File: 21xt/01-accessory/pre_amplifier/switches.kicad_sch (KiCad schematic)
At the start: 0 parts

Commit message: completed schemtic
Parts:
- added C23, C26, C28, C30, C32, C34, C36, C38, C40, C42, C44, C46, C48, C50, C52, C54: 1uF, symbol Device:C
- added C24, C25, C27, C29, C31, C33, C35, C37, C39, C41, C43, C45, C47, C49, C51, C53: 10nF, symbol Device:C
- added IC13, IC14, IC15, IC16, IC17, IC18, IC19, IC20: MAX14774ATP+, QFN50P400X400X80-21N, symbol 21xt_preamp-symbols:MAX14774ATP+
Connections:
- new net: C24.2, IC13.1 (VP)
- new net: C37.2, IC16.1 (VP)
- new net: C35.1, IC16.3 (VN)
- new net: C45.2, IC18.1 (VP)
- new net: C43.1, IC18.3 (VN)
- new net: C29.2, IC14.1 (VP)
- new net: C39.1, IC17.3 (VN)
- new net: C25.1, IC13.3 (VN)
- new net: C41.2, IC17.1 (VP)
- new net: C33.2, IC15.1 (VP)
- new net: C49.2, IC19.1 (VP)
- new net: C47.1, IC19.3 (VN)
- new net: C51.1, IC20.3 (VN)
- new net: C31.1, IC15.3 (VN)
- new net: C27.1, IC14.3 (VN)
- new net: C53.2, IC20.1 (VP)
- new net 5V: C23.1, C26.1, C28.1, C30.1, C32.1, C34.1, C36.1, C38.1, C40.1, C42.1, C44.1, C46.1, C48.1, C50.1, C52.1, C54.1, IC13.13 (VL), IC13.4 (VCC), IC14.13 (VL), IC14.4 (VCC), IC15.13 (VL), IC15.4 (VCC), IC16.13 (VL), IC16.4 (VCC), IC17.13 (VL), IC17.4 (VCC), IC18.13 (VL), IC18.4 (VCC), IC19.13 (VL), IC19.4 (VCC), IC20.13 (VL), IC20.4 (VCC)
- new net GND: C23.2, C24.1, C25.2, C26.2, C27.2, C28.2, C29.1, C30.2, C31.2, C32.2, C33.1, C34.2, C35.2, C36.2, C37.1, C38.2, C39.2, C40.2, C41.1, C42.2, C43.2, C44.2, C45.1, C46.2, C47.2, C48.2, C49.1, C50.2, C51.2, C52.2, C53.1, C54.2, IC13.2 (GND_1), IC13.21 (GND_2), IC13.5 (I.C.), IC14.2 (GND_1), IC14.21 (GND_2), IC14.5 (I.C.), IC15.2 (GND_1), IC15.21 (GND_2), IC15.5 (I.C.), IC16.2 (GND_1), IC16.21 (GND_2), IC16.5 (I.C.), IC17.2 (GND_1), IC17.21 (GND_2), IC17.5 (I.C.), IC18.2 (GND_1), IC18.21 (GND_2), IC18.5 (I.C.), IC19.2 (GND_1), IC19.21 (GND_2), IC19.5 (I.C.), IC20.2 (GND_1), IC20.21 (GND_2), IC20.5 (I.C.)
- new net P12: IC20.11 (EN1)
- new net P124_2: IC16.11 (EN1)
- new net P12_2: IC13.11 (EN1)
- new net P13: IC20.12 (EN2)
- new net P13_2: IC13.12 (EN2)
- new net P14: IC20.14 (EN3)
- new net P14_2: IC13.14 (EN3)
- new net P15: IC20.15 (EN4)
- new net P15_2: IC13.15 (EN4)
- new net P16: IC19.11 (EN1)
- new net P16_2: IC14.11 (EN1)
- new net P17: IC19.12 (EN2)
- new net P17_2: IC14.12 (EN2)
- new net P18: IC19.14 (EN3)
- new net P18_2: IC14.14 (EN3)
- new net P19: IC19.15 (EN4)
- new net P19_2: IC14.15 (EN4)
- new net P20: IC18.11 (EN1)
- new net P20_2: IC15.11 (EN1)
- new net P21: IC18.12 (EN2)
- new net P21_2: IC15.12 (EN2)
- new net P22_2: IC15.14 (EN3)
- new net P23_2: IC15.15 (EN4)
- new net P25_2: IC16.12 (EN2)
- new net P26_2: IC16.14 (EN3)
- new net P27_2: IC16.15 (EN4)
- new net P28_2: IC17.11 (EN1)
- new net P29_2: IC17.12 (EN2)
- new net P30_2: IC17.14 (EN3)
- new net P31_2: IC17.15 (EN4)
- new net Rg10_y: IC18.7 (A2)
- new net Rg10_z: IC18.19 (B2)
- new net Rg1_y: IC20.6 (A1)
- new net Rg1_z: IC20.20 (B1)
- new net Rg2_y: IC20.7 (A2)
- new net Rg2_z: IC20.19 (B2)
- new net Rg3_y: IC20.8 (A3)
- new net Rg3_z: IC20.18 (B3)
- new net Rg4_y: IC20.9 (A4)
- new net Rg4_z: IC20.17 (B4)
- new net Rg5_y: IC19.6 (A1)
- new net Rg5_z: IC19.20 (B1)
- new net Rg6_y: IC19.7 (A2)
- new net Rg6_z: IC19.19 (B2)
- new net Rg7_y: IC19.8 (A3)
- new net Rg7_z: IC19.18 (B3)
- new net Rg8_y: IC19.9 (A4)
- new net Rg8_z: IC19.17 (B4)
- new net Rg9_y: IC18.6 (A1)
- new net Rg9_z: IC18.20 (B1)
- new net Switch_x1: IC13.6 (A1)
- new net Switch_x10: IC15.7 (A2)
- new net Switch_x11: IC15.8 (A3)
- new net Switch_x12: IC15.9 (A4)
- new net Switch_x13: IC16.6 (A1)
- new net Switch_x14: IC16.7 (A2)
- new net Switch_x15: IC16.8 (A3)
- new net Switch_x16: IC16.9 (A4)
- new net Switch_x17: IC17.6 (A1)
- new net Switch_x18: IC17.7 (A2)
- new net Switch_x19: IC17.8 (A3)
- new net Switch_x2: IC13.7 (A2)
- new net Switch_x20: IC17.9 (A4)
- new net Switch_x3: IC13.8 (A3)
- new net Switch_x4: IC13.9 (A4)
- new net Switch_x5: IC14.6 (A1)
- new net Switch_x6: IC14.7 (A2)
- new net Switch_x7: IC14.8 (A3)
- new net Switch_x8: IC14.9 (A4)
- new net Switch_x9: IC15.6 (A1)
- new net Switch_y1: IC13.20 (B1)
- new net Switch_y10: IC15.19 (B2)
- new net Switch_y11: IC15.18 (B3)
- new net Switch_y12: IC15.17 (B4)
- new net Switch_y13: IC16.20 (B1)
- new net Switch_y14: IC16.19 (B2)
- new net Switch_y15: IC16.18 (B3)
- new net Switch_y16: IC16.17 (B4)
- new net Switch_y17: IC17.20 (B1)
- new net Switch_y18: IC17.19 (B2)
- new net Switch_y19: IC17.18 (B3)
- new net Switch_y2: IC13.19 (B2)
- new net Switch_y20: IC17.17 (B4)
- new net Switch_y3: IC13.18 (B3)
- new net Switch_y4: IC13.17 (B4)
- new net Switch_y5: IC14.20 (B1)
- new net Switch_y6: IC14.19 (B2)
- new net Switch_y7: IC14.18 (B3)
- new net Switch_y8: IC14.17 (B4)
- new net Switch_y9: IC15.20 (B1)
- no-connect marks 0 -> 22

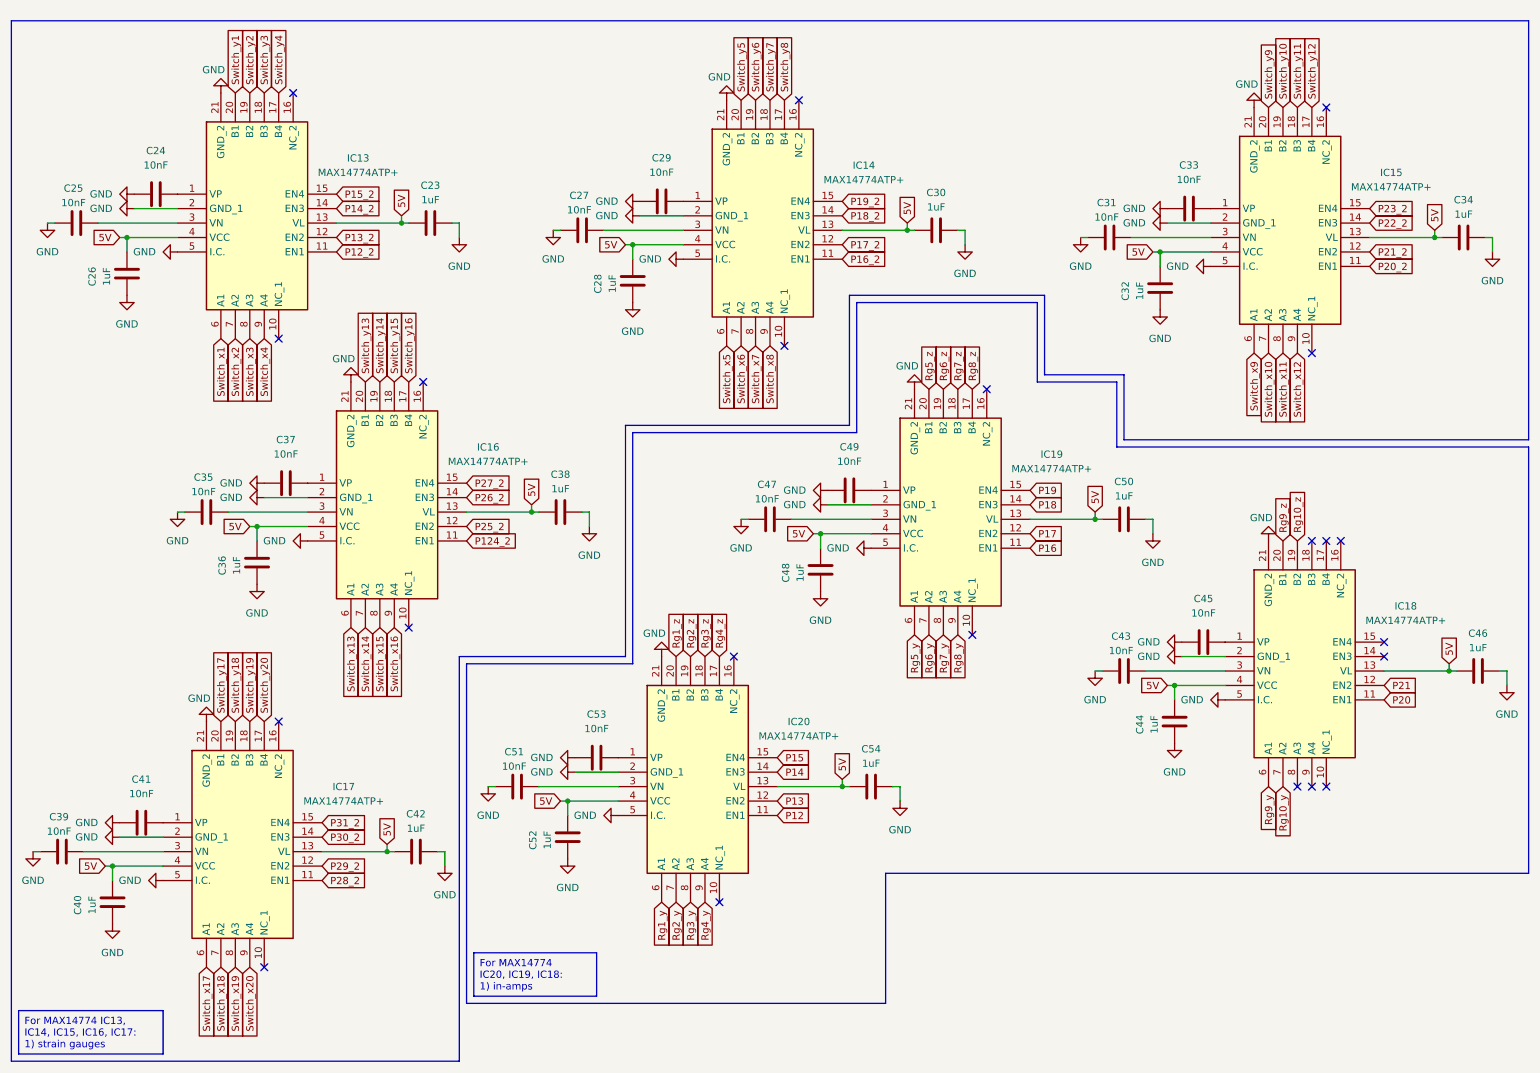
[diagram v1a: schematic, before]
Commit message: Reviewed schematic
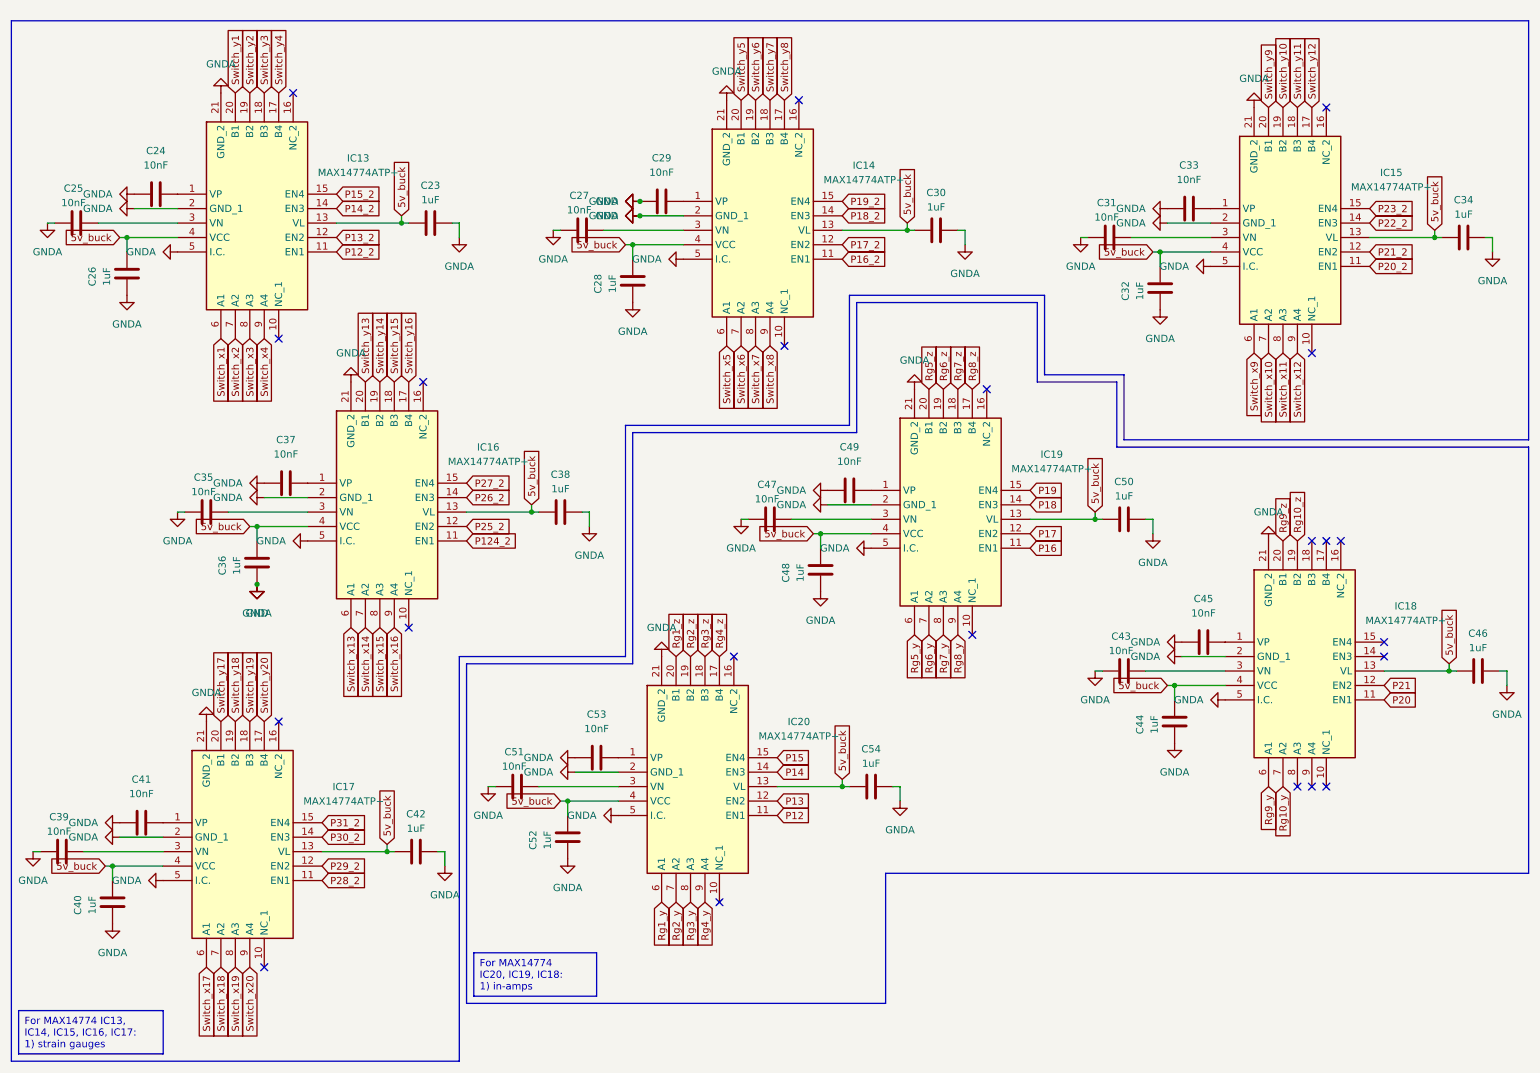
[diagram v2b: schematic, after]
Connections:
- net 5V renamed 5v_buck

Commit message: added footprints
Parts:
- IC13, IC14, IC15, IC16, IC17, IC18, IC19, IC20: footprint QFN50P400X400X80-21N -> pre_amp_footprint_lib:MAX14774ATP+_footprint
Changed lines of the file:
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@@
 			)
 		)
-		(property "Footprint" "QFN50P400X400X80-21N"
+		(property "Footprint" "pre_amp_footprint_lib:MAX14774ATP+_footprint"
 			(at 252.73 207.95 0)
 			(effects
@@
 			)
 		)
-		(property "Footprint" "QFN50P400X400X80-21N"
+		(property "Footprint" "pre_amp_footprint_lib:MAX14774ATP+_footprint"
 			(at 91.44 180.01 0)
 			(effects
@@
 			)
 		)
-		(property "Footprint" "QFN50P400X400X80-21N"
+		(property "Footprint" "pre_amp_footprint_lib:MAX14774ATP+_footprint"
 			(at 68.58 129.21 0)
 			(effects
@@
 			)
 		)
-		(property "Footprint" "QFN50P400X400X80-21N"
+		(property "Footprint" "pre_amp_footprint_lib:MAX14774ATP+_footprint"
 			(at 190.5 181.28 0)
 			(effects
@@
 			)
 		)
-		(property "Footprint" "QFN50P400X400X80-21N"
+		(property "Footprint" "pre_amp_footprint_lib:MAX14774ATP+_footprint"
 			(at 66.04 239.7 0)
 			(effects
@@
 			)
 		)
-		(property "Footprint" "QFN50P400X400X80-21N"
+		(property "Footprint" "pre_amp_footprint_lib:MAX14774ATP+_footprint"
 			(at 250.19 131.75 0)
 			(effects
@@
 			)
 		)
-		(property "Footprint" "QFN50P400X400X80-21N"
+		(property "Footprint" "pre_amp_footprint_lib:MAX14774ATP+_footprint"
 			(at 157.48 130.48 0)
 			(effects
@@
 			)
 		)
-		(property "Footprint" "QFN50P400X400X80-21N"
+		(property "Footprint" "pre_amp_footprint_lib:MAX14774ATP+_footprint"
 			(at 146.05 228.27 0)
 			(effects

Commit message: added footprints
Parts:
- IC13, IC14, IC15, IC16, IC17, IC18, IC19, IC20: footprint pre_amp_footprint_lib:MAX14774ATP+_footprint -> 21xt_footprints:MAX14774ATP_
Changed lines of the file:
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@@
 			)
 		)
-		(property "Footprint" "pre_amp_footprint_lib:MAX14774ATP+_footprint"
+		(property "Footprint" "21xt_footprints:MAX14774ATP_"
 			(at 252.73 207.95 0)
 			(effects
@@
 			)
 		)
-		(property "Footprint" "pre_amp_footprint_lib:MAX14774ATP+_footprint"
+		(property "Footprint" "21xt_footprints:MAX14774ATP_"
 			(at 91.44 180.01 0)
 			(effects
@@
 			)
 		)
-		(property "Footprint" "pre_amp_footprint_lib:MAX14774ATP+_footprint"
+		(property "Footprint" "21xt_footprints:MAX14774ATP_"
 			(at 68.58 129.21 0)
 			(effects
@@
 			)
 		)
-		(property "Footprint" "pre_amp_footprint_lib:MAX14774ATP+_footprint"
+		(property "Footprint" "21xt_footprints:MAX14774ATP_"
 			(at 190.5 181.28 0)
 			(effects
@@
 			)
 		)
-		(property "Footprint" "pre_amp_footprint_lib:MAX14774ATP+_footprint"
+		(property "Footprint" "21xt_footprints:MAX14774ATP_"
 			(at 66.04 239.7 0)
 			(effects
@@
 			)
 		)
-		(property "Footprint" "pre_amp_footprint_lib:MAX14774ATP+_footprint"
+		(property "Footprint" "21xt_footprints:MAX14774ATP_"
 			(at 250.19 131.75 0)
 			(effects
@@
 			)
 		)
-		(property "Footprint" "pre_amp_footprint_lib:MAX14774ATP+_footprint"
+		(property "Footprint" "21xt_footprints:MAX14774ATP_"
 			(at 157.48 130.48 0)
 			(effects
@@
 			)
 		)
-		(property "Footprint" "pre_amp_footprint_lib:MAX14774ATP+_footprint"
+		(property "Footprint" "21xt_footprints:MAX14774ATP_"
 			(at 146.05 228.27 0)
 			(effects

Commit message: assigned footprints
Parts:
- C23, C24, C25, C26, C27, C28, C29, C30, C31, C32, C33, C34, C35, C36, C37, C38, C39, C40, C41, C42, C43, C44, C45, C46, C47, C48, C49, C50, C51, C52, C53, C54: footprint (none) -> Capacitor_SMD:C_0402_1005Metric
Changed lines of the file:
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@@
 			)
 		)
-		(property "Footprint" ""
+		(property "Footprint" "Capacitor_SMD:C_0402_1005Metric"
 			(at 36.5252 62.23 0)
 			(effects
@@
 			)
 		)
-		(property "Footprint" ""
+		(property "Footprint" "Capacitor_SMD:C_0402_1005Metric"
 			(at 44.45 43.4848 0)
 			(effects
@@
 			)
 		)
-		(property "Footprint" ""
+		(property "Footprint" "Capacitor_SMD:C_0402_1005Metric"
 			(at 67.31 94.2848 0)
 			(effects
@@
 			)
 		)
-		(property "Footprint" ""
+		(property "Footprint" "Capacitor_SMD:C_0402_1005Metric"
 			(at 181.61 49.8348 0)
 			(effects
@@
 			)
 		)
-		(property "Footprint" ""
+		(property "Footprint" "Capacitor_SMD:C_0402_1005Metric"
 			(at 45.72 101.2952 0)
 			(effects
@@
 			)
 		)
-		(property "Footprint" ""
+		(property "Footprint" "Capacitor_SMD:C_0402_1005Metric"
 			(at 133.35 44.7548 0)
 			(effects
@@
 			)
 		)
-		(property "Footprint" ""
+		(property "Footprint" "Capacitor_SMD:C_0402_1005Metric"
 			(at 113.9952 161.29 0)
 			(effects
@@
 			)
 		)
-		(property "Footprint" ""
+		(property "Footprint" "Capacitor_SMD:C_0402_1005Metric"
 			(at 228.6 122.2248 0)
 			(effects
@@
 			)
 		)
-		(property "Footprint" ""
+		(property "Footprint" "Capacitor_SMD:C_0402_1005Metric"
 			(at 276.86 127.3048 0)
 			(effects
@@
 			)
 		)
-		(property "Footprint" ""
+		(property "Footprint" "Capacitor_SMD:C_0402_1005Metric"
 			(at 115.57 99.3648 0)
 			(effects
@@
 			)
 		)
-		(property "Footprint" ""
+		(property "Footprint" "Capacitor_SMD:C_0402_1005Metric"
 			(at 20.32 160.9852 0)
 			(effects
@@
 			)
 		)
-		(property "Footprint" ""
+		(property "Footprint" "Capacitor_SMD:C_0402_1005Metric"
 			(at 41.91 153.9748 0)
 			(effects
@@
 			)
 		)
-		(property "Footprint" ""
+		(property "Footprint" "Capacitor_SMD:C_0402_1005Metric"
 			(at 226.06 46.0248 0)
 			(effects
@@
 			)
 		)
-		(property "Footprint" ""
+		(property "Footprint" "Capacitor_SMD:C_0402_1005Metric"
 			(at 214.63 100.6348 0)
 			(effects
@@
 			)
 		)
-		(property "Footprint" ""
+		(property "Footprint" "Capacitor_SMD:C_0402_1005Metric"
 			(at 166.37 95.5548 0)
 			(effects
@@
 			)
 		)
-		(property "Footprint" ""
+		(property "Footprint" "Capacitor_SMD:C_0402_1005Metric"
 			(at 218.1352 64.77 0)
 			(effects
@@
 			)
 		)
-		(property "Footprint" ""
+		(property "Footprint" "Capacitor_SMD:C_0402_1005Metric"
 			(at 125.4252 63.5 0)
 			(effects
@@
 			)
 		)
-		(property "Footprint" ""
+		(property "Footprint" "Capacitor_SMD:C_0402_1005Metric"
 			(at 33.9852 172.72 0)
 			(effects
@@
 			)
 		)
-		(property "Footprint" ""
+		(property "Footprint" "Capacitor_SMD:C_0402_1005Metric"
 			(at 59.3852 113.03 0)
 			(effects
@@
 			)
 		)
-		(property "Footprint" ""
+		(property "Footprint" "Capacitor_SMD:C_0402_1005Metric"
 			(at 100.33 149.5552 0)
 			(effects
@@
 			)
 		)
-		(property "Footprint" ""
+		(property "Footprint" "Capacitor_SMD:C_0402_1005Metric"
 			(at 207.01 129.2352 0)
 			(effects
@@
 			)
 		)
-		(property "Footprint" ""
+		(property "Footprint" "Capacitor_SMD:C_0402_1005Metric"
 			(at 158.4452 114.3 0)
 			(effects
@@
 			)
 		)
-		(property "Footprint" ""
+		(property "Footprint" "Capacitor_SMD:C_0402_1005Metric"
 			(at 92.71 48.5648 0)
 			(effects
@@
 			)
 		)
-		(property "Footprint" ""
+		(property "Footprint" "Capacitor_SMD:C_0402_1005Metric"
 			(at 90.17 159.0548 0)
 			(effects
@@
 			)
 		)
-		(property "Footprint" ""
+		(property "Footprint" "Capacitor_SMD:C_0402_1005Metric"
 			(at 170.18 147.6248 0)
 			(effects
@@
 			)
 		)
-		(property "Footprint" ""
+		(property "Footprint" "Capacitor_SMD:C_0402_1005Metric"
 			(at 144.78 102.5652 0)
 			(effects
@@
 			)
 		)
-		(property "Footprint" ""
+		(property "Footprint" "Capacitor_SMD:C_0402_1005Metric"
 			(at 121.92 142.5448 0)
 			(effects
@@
 			)
 		)
-		(property "Footprint" ""
+		(property "Footprint" "Capacitor_SMD:C_0402_1005Metric"
 			(at 204.47 53.0352 0)
 			(effects
@@
 			)
 		)
-		(property "Footprint" ""
+		(property "Footprint" "Capacitor_SMD:C_0402_1005Metric"
 			(at 274.32 51.1048 0)
 			(effects
@@
 			)
 		)
-		(property "Footprint" ""
+		(property "Footprint" "Capacitor_SMD:C_0402_1005Metric"
 			(at 220.6752 140.97 0)
 			(effects
@@
 			)
 		)
-		(property "Footprint" ""
+		(property "Footprint" "Capacitor_SMD:C_0402_1005Metric"
 			(at 22.86 50.4952 0)
 			(effects
@@
 			)
 		)
-		(property "Footprint" ""
+		(property "Footprint" "Capacitor_SMD:C_0402_1005Metric"
 			(at 111.76 51.7652 0)
 			(effects

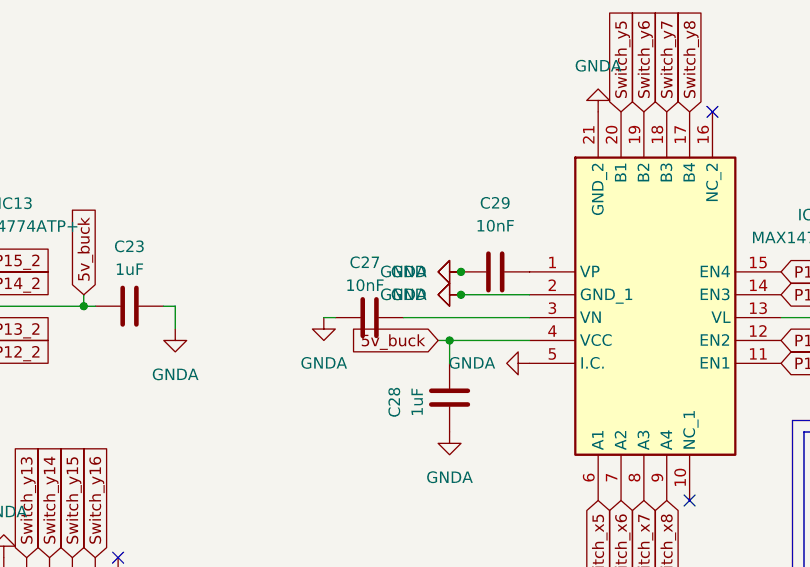
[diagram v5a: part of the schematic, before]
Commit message: slight symbol edits
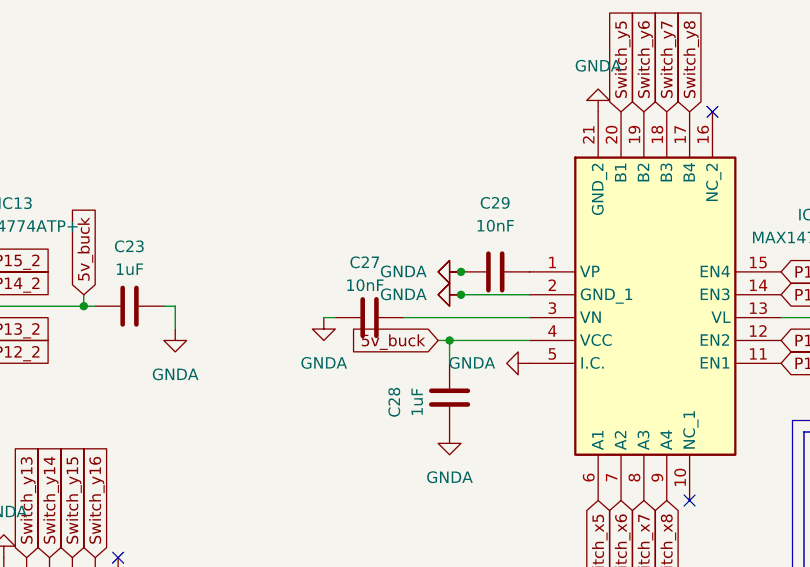
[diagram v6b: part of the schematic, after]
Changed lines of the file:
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@@
 				)
 				(justify right)
+				(hide yes)
 			)
 		)
@@
 		(on_board yes)
 		(dnp no)
-		(fields_autoplaced yes)
 		(property "Reference" "#PWR061"
 			(at 119.38 45.72 0)
@@
 			)
 		)
-		(property "Value" "GND"
+		(property "Value" "GNDA"
 			(at 121.92 45.7199 90)
 			(effects
@@
 				)
 				(justify right)
+				(hide yes)
 			)
 		)

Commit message: fixing inputs
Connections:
- net P124_2 renamed P24_2
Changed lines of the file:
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@@
 		)
 	)
-	(global_label "P124_2"
+	(global_label "P24_2"
 		(shape input)
 		(at 95.25 105.41 0)
@@
 		)
 		(property "Intersheetrefs" "${INTERSHEET_REFS}"
-			(at 105.3108 105.41 0)
+			(at 104.1013 105.41 0)
 			(effects
 				(font
